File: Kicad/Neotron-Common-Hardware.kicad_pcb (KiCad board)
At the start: 2 copper layers, 243.8 x 243.8 mm, 124 parts, among them J201 DB15_Female_HighDensity_Mount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, J301 RJ45_Amphenol_RJMG1BD3B8K1ANR, J401 CD Audio In, J402 AC'97 Audio Header, J403 Line Out, J501 USB_A_x2, J601 USB_B, J701 Double-mini-DIN-6, J801 Conn_02x05, J802 DB9_Male_MountingHoles, J901 DB9_Female_MountingHoles, U301 ENC424J600-PT, U401 TLV320AIC23BPW, U402 STX-4335-5BGP-S1, U801 ST3232CDR, Y301 25M, Y401 12M

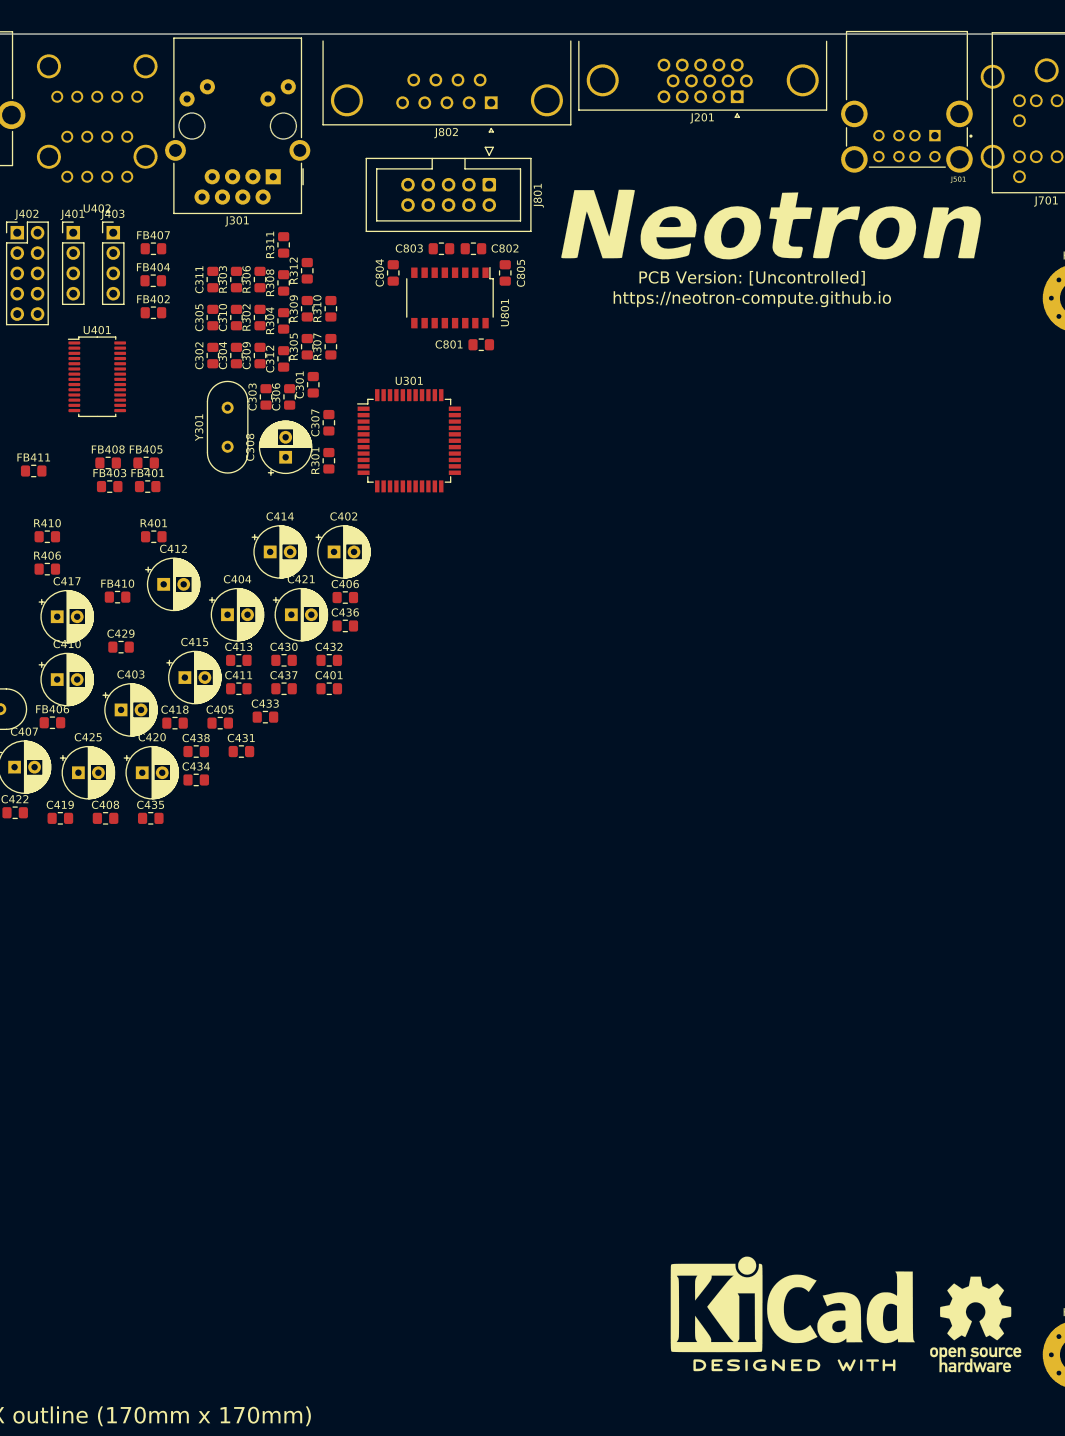
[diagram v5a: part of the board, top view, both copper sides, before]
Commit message: Working on VGA sheet and USB sheet.
Also added courtyard and silk to stacked USB connector.
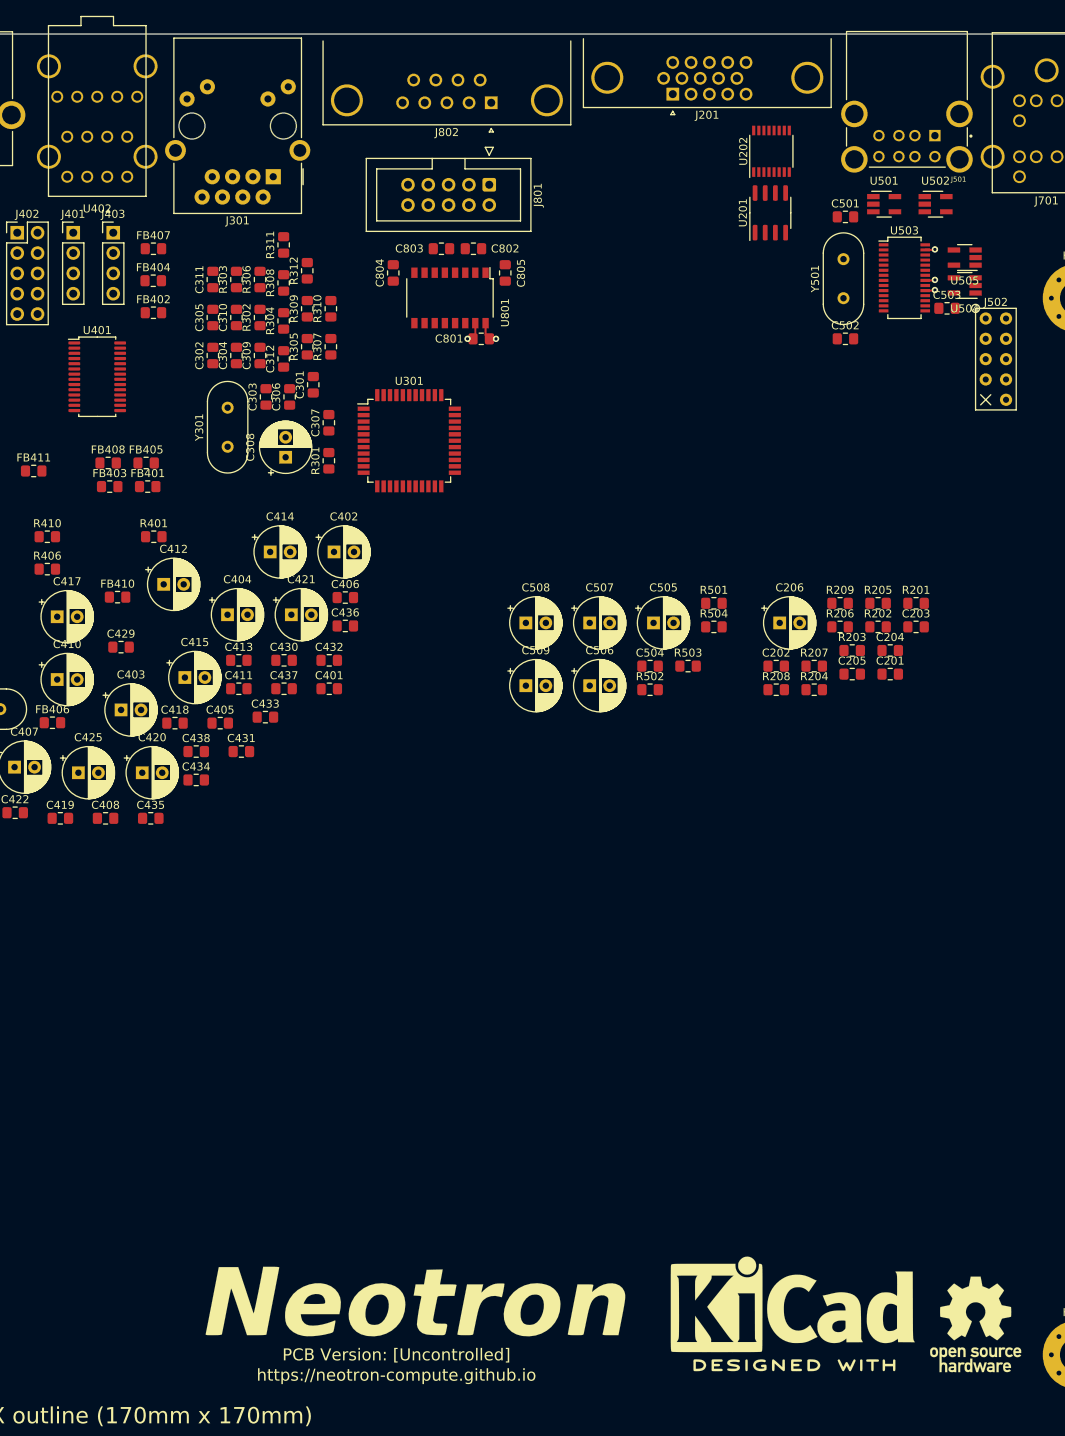
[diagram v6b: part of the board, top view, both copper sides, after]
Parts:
- added C201: 220n, Capacitor_SMD:C_0805_2012Metric_Pad1.15x1.40mm_HandSolder, F.Cu at (247.9, 111.2)
- added C202: 100n, Capacitor_SMD:C_0805_2012Metric_Pad1.15x1.40mm_HandSolder, F.Cu at (233.6, 110.2)
- added C203: 100n, Capacitor_SMD:C_0805_2012Metric_Pad1.15x1.40mm_HandSolder, F.Cu at (251.1, 105.3)
- added C204: 100n, Capacitor_SMD:C_0805_2012Metric_Pad1.15x1.40mm_HandSolder, F.Cu at (247.9, 108.2)
- added C205: 100n, Capacitor_SMD:C_0805_2012Metric_Pad1.15x1.40mm_HandSolder, F.Cu at (243.1, 111.2)
- added C206: 10u, Capacitor_THT:CP_Radial_D6.3mm_P2.50mm, F.Cu at (234.1, 104.8)
- added C501: 12p, Capacitor_SMD:C_0805_2012Metric_Pad1.15x1.40mm_HandSolder, F.Cu at (242.3, 54.0)
- added C502: 12p, Capacitor_SMD:C_0805_2012Metric_Pad1.15x1.40mm_HandSolder, F.Cu at (242.3, 69.3)
- added C503: 100n, Capacitor_SMD:C_0805_2012Metric_Pad1.15x1.40mm_HandSolder, F.Cu at (255.0, 65.5)
- added C504: 100n, Capacitor_SMD:C_0805_2012Metric_Pad1.15x1.40mm_HandSolder, F.Cu at (217.9, 110.2)
- added C505: 4u7, Capacitor_THT:CP_Radial_D6.3mm_P2.50mm, F.Cu at (218.3, 104.8)
- added C506: 120u, Capacitor_THT:CP_Radial_D6.3mm_P2.50mm, F.Cu at (210.3, 112.6)
- added C507: 120u, Capacitor_THT:CP_Radial_D6.3mm_P2.50mm, F.Cu at (210.3, 104.8)
- added C508: 120u, Capacitor_THT:CP_Radial_D6.3mm_P2.50mm, F.Cu at (202.3, 104.8)
- added C509: 120u, Capacitor_THT:CP_Radial_D6.3mm_P2.50mm, F.Cu at (202.3, 112.6)
- added J502: USB Ports Internal, Neotron-Common-Hardware:USB_Header, F.Cu at (261.1, 64.2)
- added R201: 75, Resistor_SMD:R_0805_2012Metric_Pad1.15x1.40mm_HandSolder, F.Cu at (251.1, 102.3)
- added R202: 75, Resistor_SMD:R_0805_2012Metric_Pad1.15x1.40mm_HandSolder, F.Cu at (246.4, 105.3)
- added R203: 75, Resistor_SMD:R_0805_2012Metric_Pad1.15x1.40mm_HandSolder, F.Cu at (243.1, 108.2)
- added R204: 10k, Resistor_SMD:R_0805_2012Metric_Pad1.15x1.40mm_HandSolder, F.Cu at (238.4, 113.1)
- added R205: 10k, Resistor_SMD:R_0805_2012Metric_Pad1.15x1.40mm_HandSolder, F.Cu at (246.4, 102.3)
- added R206: 10k, Resistor_SMD:R_0805_2012Metric_Pad1.15x1.40mm_HandSolder, F.Cu at (241.6, 105.3)
- added R207: 1k5, Resistor_SMD:R_0805_2012Metric_Pad1.15x1.40mm_HandSolder, F.Cu at (238.4, 110.2)
- added R208: 1k5, Resistor_SMD:R_0805_2012Metric_Pad1.15x1.40mm_HandSolder, F.Cu at (233.6, 113.1)
- added R209: DNP, Resistor_SMD:R_0805_2012Metric_Pad1.15x1.40mm_HandSolder, F.Cu at (241.6, 102.3)
- added R501: 2k7 1%, Resistor_SMD:R_0805_2012Metric_Pad1.15x1.40mm_HandSolder, F.Cu at (225.8, 102.3)
- added R502: 10k, Resistor_SMD:R_0805_2012Metric_Pad1.15x1.40mm_HandSolder, F.Cu at (217.9, 113.1)
- added R503: 100k, Resistor_SMD:R_0805_2012Metric_Pad1.15x1.40mm_HandSolder, F.Cu at (222.6, 110.2)
- added R504: 10k, Resistor_SMD:R_0805_2012Metric_Pad1.15x1.40mm_HandSolder, F.Cu at (225.8, 105.3)
- added U201: TPF133A, Package_SO:SOIC-8_3.9x4.9mm_P1.27mm, F.Cu at (232.9, 53.5)
- added U202: TPD7S019, Package_SO:SSOP-16_3.9x4.9mm_P0.635mm, F.Cu at (233.0, 45.8)
- added U501: MIC2005A-2YM5, Package_TO_SOT_SMD:SOT-23-5_HandSoldering, F.Cu at (247.1, 52.5)
- added U502: MIC2005A-2YM5, Package_TO_SOT_SMD:SOT-23-5_HandSoldering, F.Cu at (253.6, 52.5)
- added U503: XR22404CG28, Package_SO:SSOP-28_3.9x9.9mm_P0.635mm, F.Cu at (249.7, 61.7)
- added U504: MIC2005A-2YM5, Package_TO_SOT_SMD:SOT-23-5_HandSoldering, F.Cu at (257.2, 62.6)
- added U505: MIC2005A-2YM5, Package_TO_SOT_SMD:SOT-23-5_HandSoldering, F.Cu at (257.2, 59.1)
- added Y501: 12M, Crystal:Crystal_HC49-4H_Vertical, F.Cu at (242.0, 64.2)
- J201: value DB15_Female_HighDensity_MountingHoles -> DE15HD; footprint Connector_Dsub:DSUB-15-HD_Male_Horizontal_P2.29x1.98mm_EdgePinOffset3.03mm_Housed_MountingHolesOffset4.94mm -> Connector_Dsub:DSUB-15-HD_Female_Horizontal_P2.29x1.98mm_EdgePinOffset3.03mm_Housed_MountingHolesOffset4.94mm
- J501: value USB_A_x2 -> USB Ports External
- moved LOGO103 141.8 mm to (188.7, 189.9)
- moved J201 8.07 mm to (220.7, 38.7)
- moved C801 0.74 mm to (196.8, 69.3)
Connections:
- FB403 pad 2: (no net) -> +5V
- J201 pad 1: (no net) -> /Video/VGA_RED
- J201 pad 10: (no net) -> GND
- J201 pad 12: (no net) -> /Video/VGA_DDC_SDA
- J201 pad 13: (no net) -> /Video/VGA_HSYNC
- J201 pad 14: (no net) -> /Video/VGA_VSYNC
- J201 pad 15: (no net) -> /Video/VGA_DDC_SCL
- J201 pad 2: (no net) -> /Video/VGA_GRN
- J201 pad 3: (no net) -> /Video/VGA_BLU
- J201 pad 5: (no net) -> GND
- J201 pad 6: (no net) -> GND
- J201 pad 7: (no net) -> GND
- J201 pad 8: (no net) -> GND
- J201 pad 9: (no net) -> +5V
- J501 pad 1: (no net) -> Net-(C506-Pad1)
- J501 pad 2: (no net) -> /USB/USBD1+
- J501 pad 3: (no net) -> /USB/USBD1-
- J501 pad 4: (no net) -> GND
- J501 pad 5: (no net) -> Net-(C507-Pad1)
- J501 pad 6: (no net) -> /USB/USBD2+
- J501 pad 7: (no net) -> /USB/USBD2-
- J501 pad 8: (no net) -> GND
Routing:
- net +3V3: track 0.00 -> 5.98 mm, vias 0 -> 4
- net GND: track 0.00 -> 2.08 mm, vias 0 -> 1
- added copper zone on In2.Cu, net +3V3
- added copper zone on In1.Cu, net GND
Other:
- copper layers 2 -> 4
